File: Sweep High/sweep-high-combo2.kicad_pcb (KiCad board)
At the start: 2 copper layers, 229.5 x 95.2 mm, 42 parts, among them J1 AudioJack4dpb, J2 AudioJack4dpb, SW10 SW_Push, SW11 SW_Push, SW11_r1 SW_Push, SW12 SW_Push, SW12_r1 SW_Push, SW13_r1 SW_Push, SW14 SW_Push, SW15 SW_Push, SW15_r1 SW_Push, SW16 SW_Push, SW16_r1 SW_Push, SW17 SW_Push, SW17_r1 SW_Push, SW18 SW_Push, SW18_r1 SW_Push, SW2 SW_Push, SW20 SW_Push, SW20_r1 SW_Push, SW21 SW_Push, SW21_r1 SW_Push, SW2_r1 SW_Push, SW3 SW_Push, SW3_r1 SW_Push, SW4 SW_Push, SW4_r1 SW_Push, SW5 SW_Push, SW5_r1 SW_Push, SW6 SW_Push, SW6_r1 SW_Push, SW7_r1 SW_Push, SW8 SW_Push, SW8_r1 SW_Push, SW9 SW_Push, SW9_r1 SW_Push, U1 ProMicro-kbd, U2 ProMicro-kbd

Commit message: Add shater PCB, update gerbers
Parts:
- moved G*** 0.93 mm to (214.3, 84.9)
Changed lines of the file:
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@@
   )
   (footprint "silkscreens:safe_rust" (layer "B.Cu")
-    (at 213.717152 84.167888 -171)
+    (at 214.327152 84.867888 -171)
     (attr exclude_from_pos_files exclude_from_bom)
     (fp_text reference "G***" (at 0 0 9) (layer "B.SilkS") hide

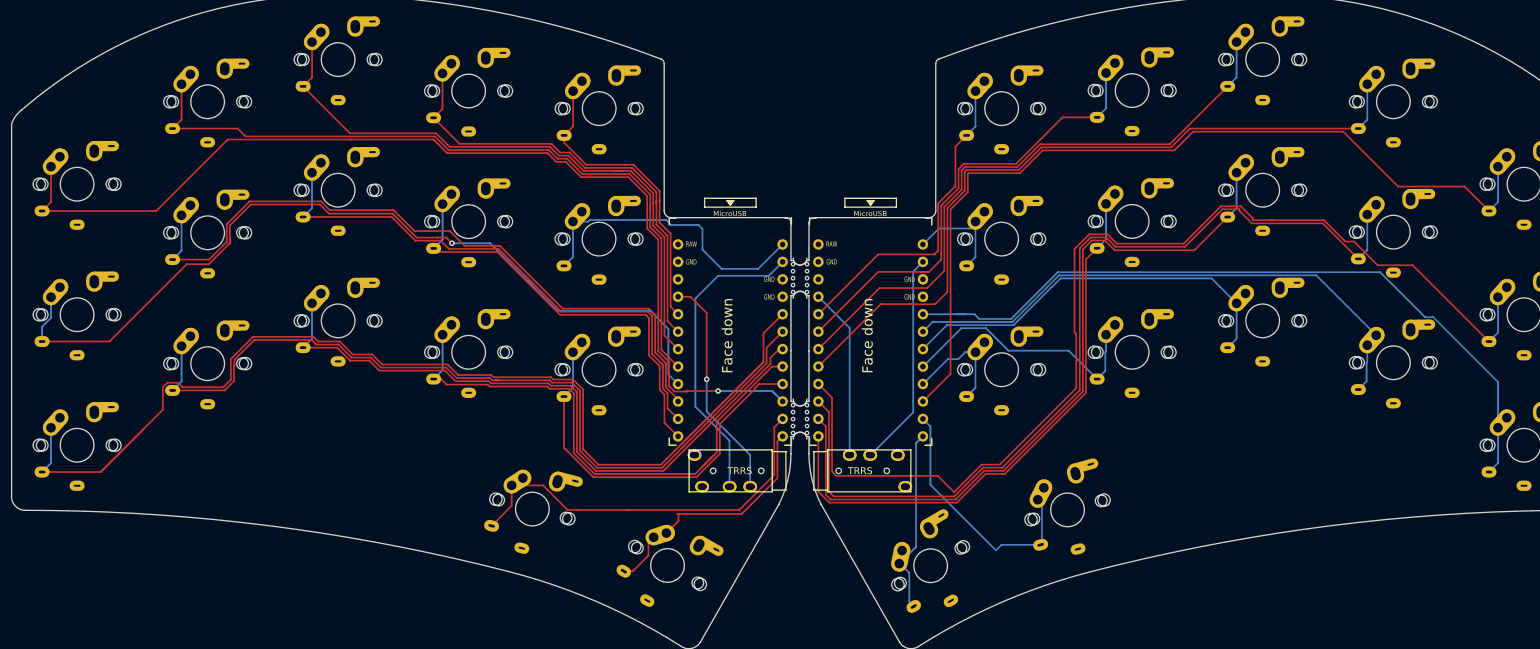
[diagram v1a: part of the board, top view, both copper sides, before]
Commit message: Add splinter pcb
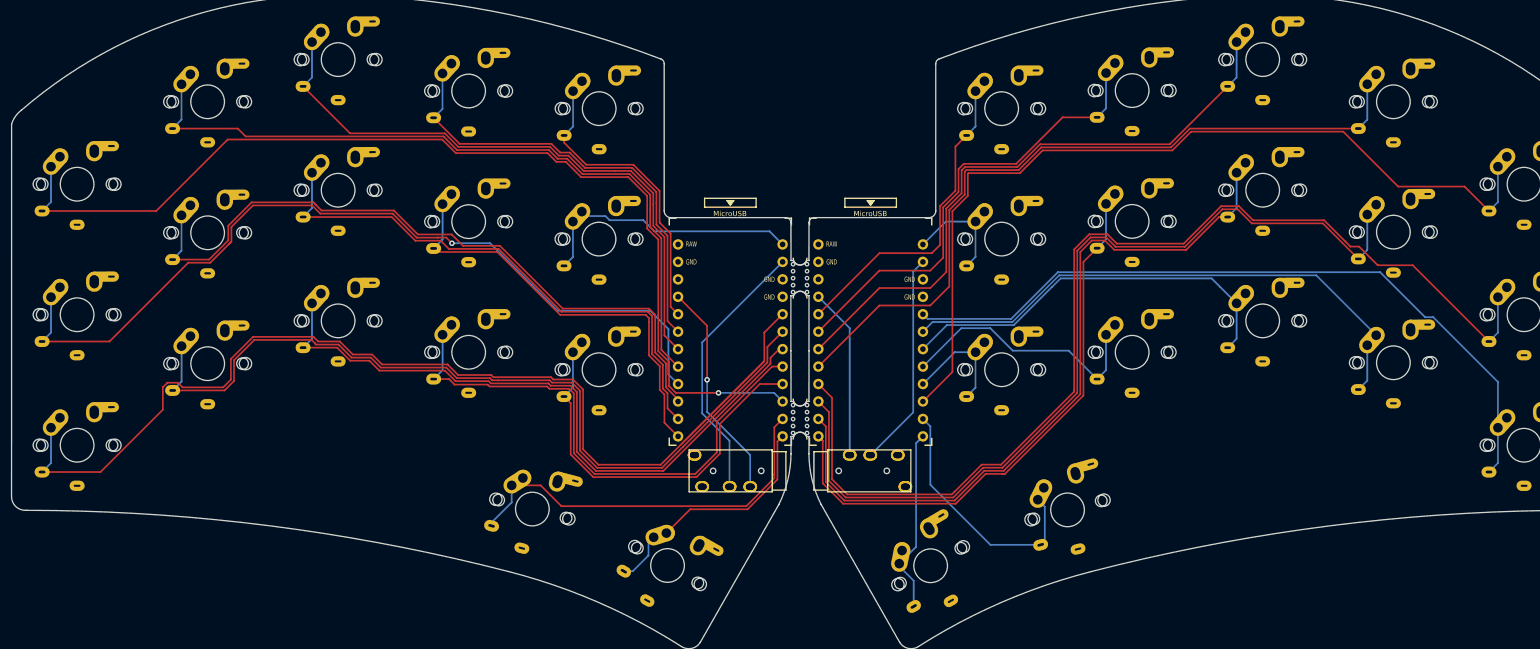
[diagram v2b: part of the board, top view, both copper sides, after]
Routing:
- net Switch11: track 178.4 -> 168.4 mm
- net Switch10: track 43.8 -> 38.2 mm
- net Switch18: track 44.4 -> 39.2 mm
- net Switch14: track 80.0 -> 77.7 mm
- net Switch6: track 125.8 -> 123.8 mm
- net Switch3: track 89.9 -> 88.6 mm
- net Switch11_r: track 108.4 -> 107.1 mm
- net Switch1: track 150.4 -> 149.2 mm
- net vcc: track 58.0 -> 56.9 mm
- net Switch8_r: track 107.6 -> 106.6 mm
- net Switch7_r: track 131.8 -> 130.9 mm
- net Switch9_r: track 83.3 -> 82.4 mm
- net gnd: track 0.75 -> 0.00 mm
- net Switch17: track 34.2 -> 33.5 mm
- net Switch16: track 58.2 -> 57.5 mm
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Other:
- board text removed: "Face down"
